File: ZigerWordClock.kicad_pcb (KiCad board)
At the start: 2 copper layers, 237 x 237 mm, 21 parts, among them U1 BH1750, U10 BTF-5V-060L-B_SK9822_LED_Stri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, U11 BTF-5V-060L-B_SK9822_LED_Stri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, U12 BTF-5V-060L-B_SK9822_LED_Stri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, U13 BTF-5V-060L-B_SK9822_LED_Stri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, U14 BTF-5V-060L-B_SK9822_LED_Stri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, U15 BTF-5V-060L-B_SK9822_LED_Stri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, U16 BTF-5V-060L-B_SK9822_LED_Stri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, U17 BTF-5V-060L-B_SK9822_LED_Stri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, U18 BTF-5V-060L-B_SK9822_LED_Stri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, U19 BTF-5V-060L-B_SK9822_LED_Stri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, U2 LILYGO(R)_TTGO_T8_ESP32-S2_V1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, U3 BTF-5V-060L-B_SK9822_LED_Stri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, U4 LevelShifter, U5 BTF-5V-060L-B_SK9822_LED_Stri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, U6 BTF-5V-060L-B_SK9822_LED_Stri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, U7 BTF-5V-060L-B_SK9822_LED_Stri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, U8 BTF-5V-060L-B_SK9822_LED_Stri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, U9 BTF-5V-060L-B_SK9822_LED_Stri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

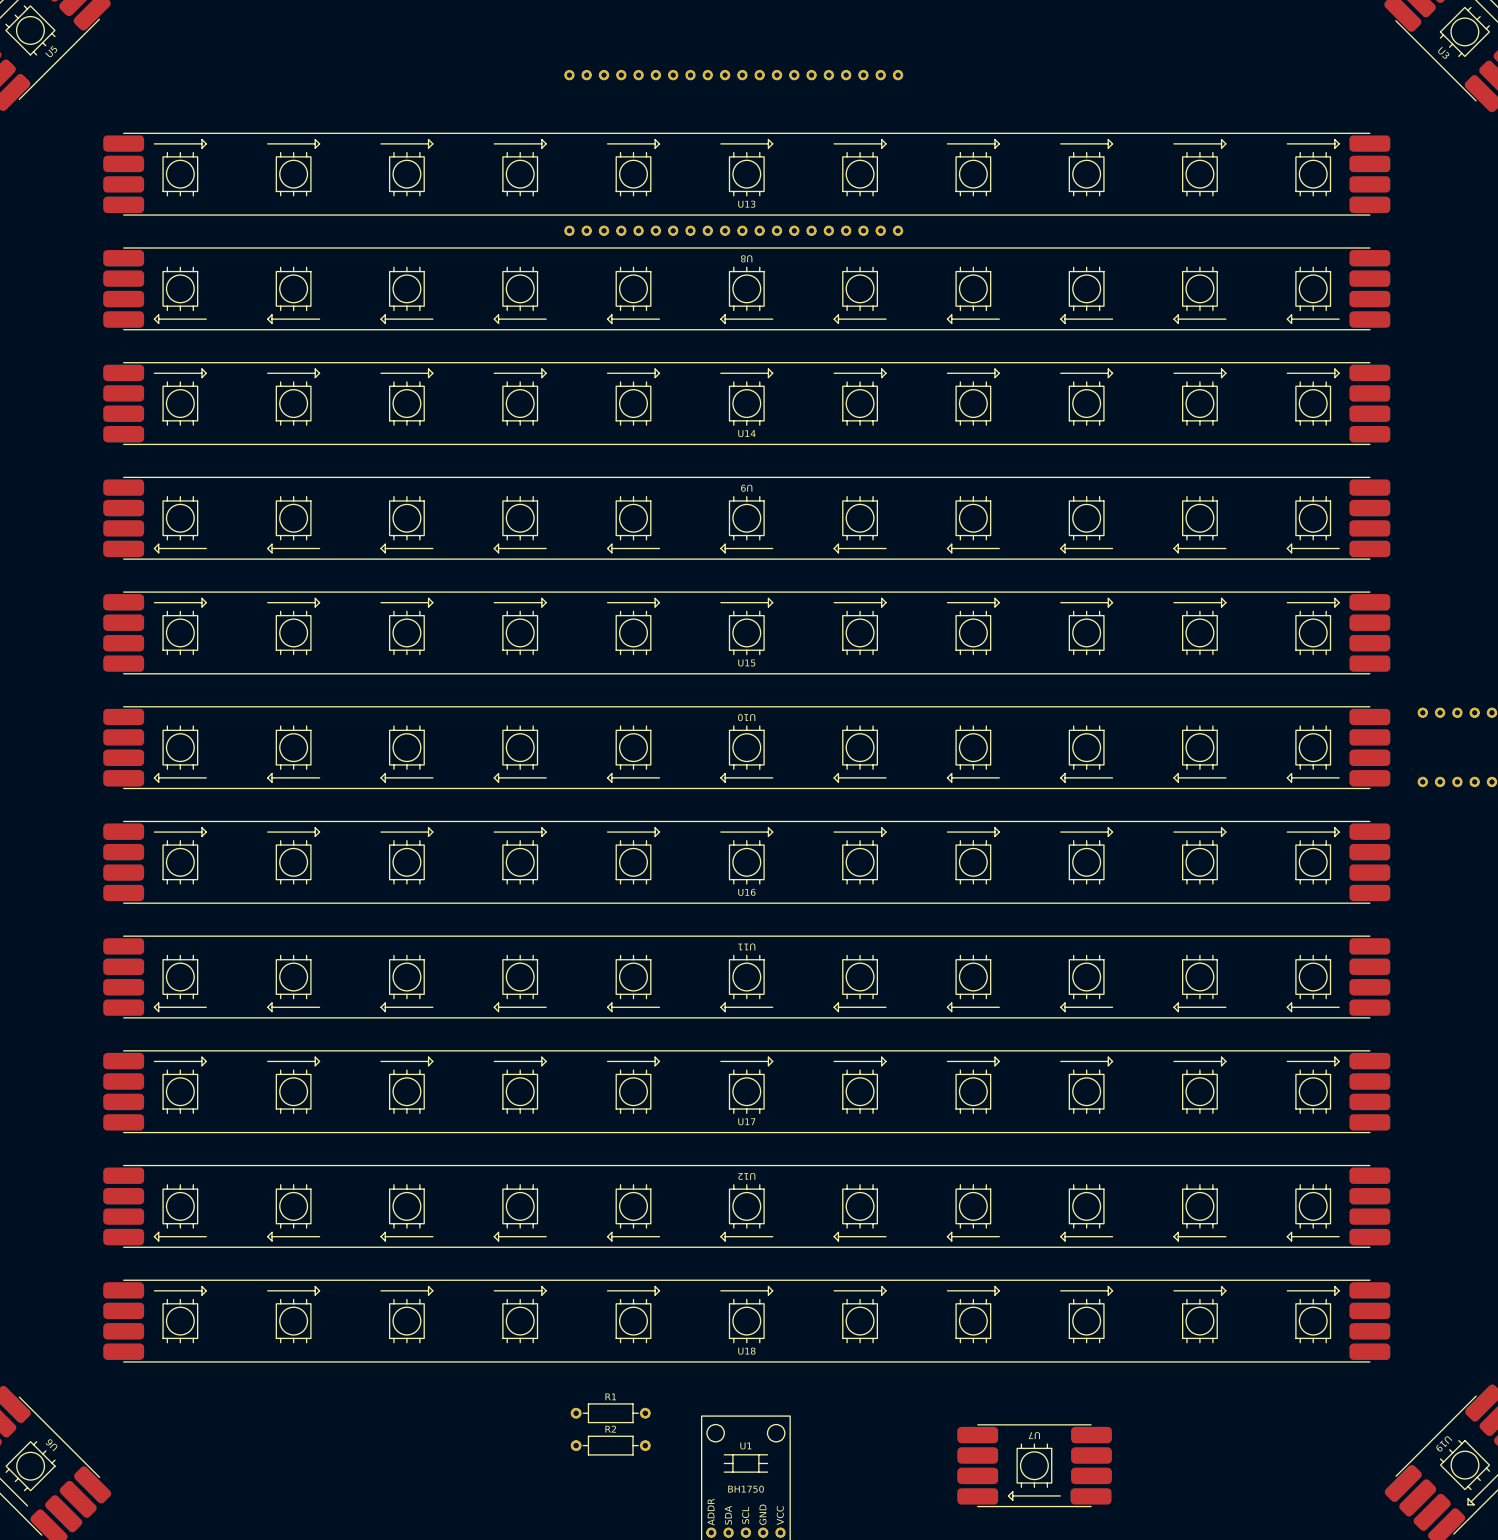
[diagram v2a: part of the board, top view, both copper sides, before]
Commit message: Adds ir receiver to schematic and board
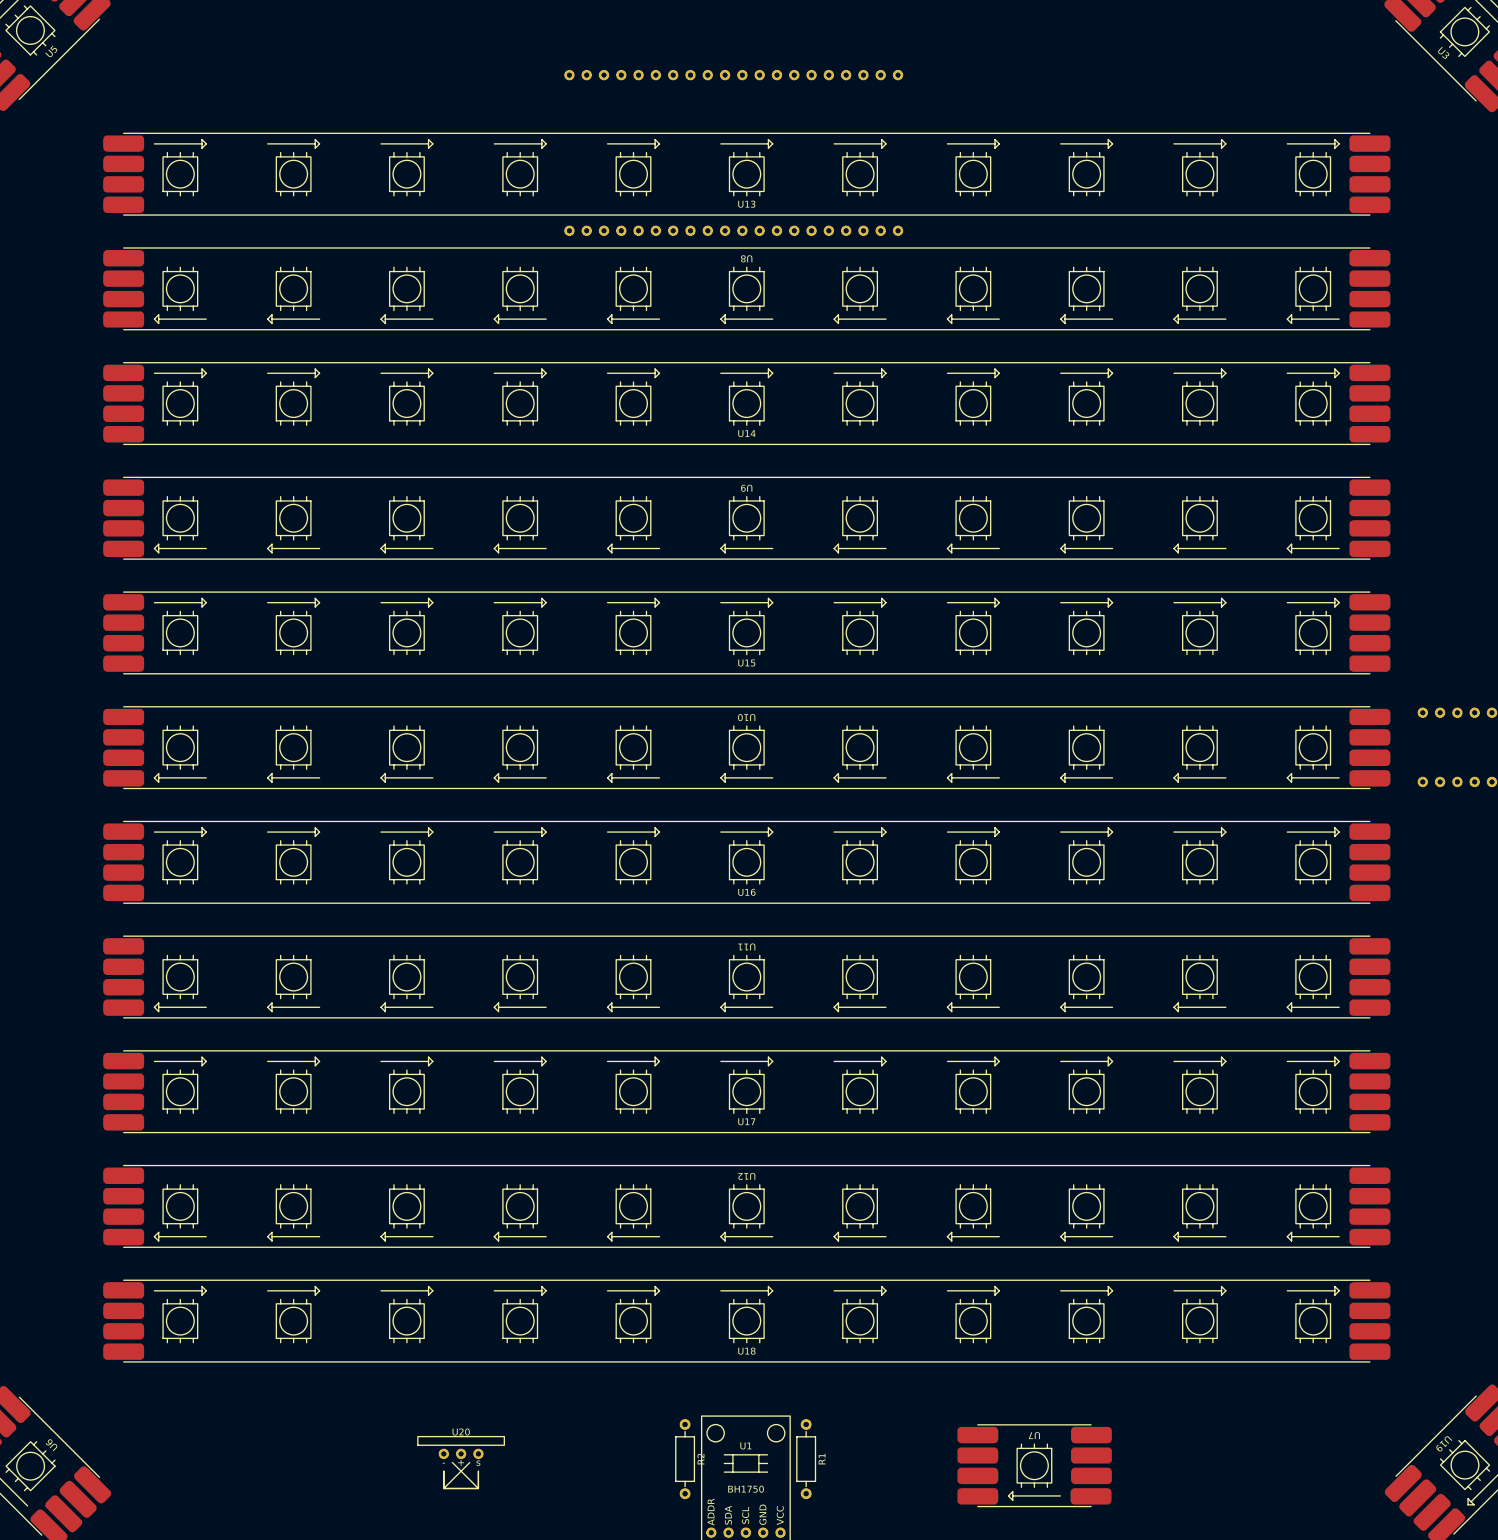
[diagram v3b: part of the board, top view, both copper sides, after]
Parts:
- added U20: IR-Module_38KHz, WordClock Footprint Library:IR-Module_38KHz, F.Cu at (118.2, 250.7)
- moved R1 33.8 mm to (168.9, 248.9), turned to -90 degrees
- moved R2 16.3 mm to (151.1, 248.9), turned to -90 degrees

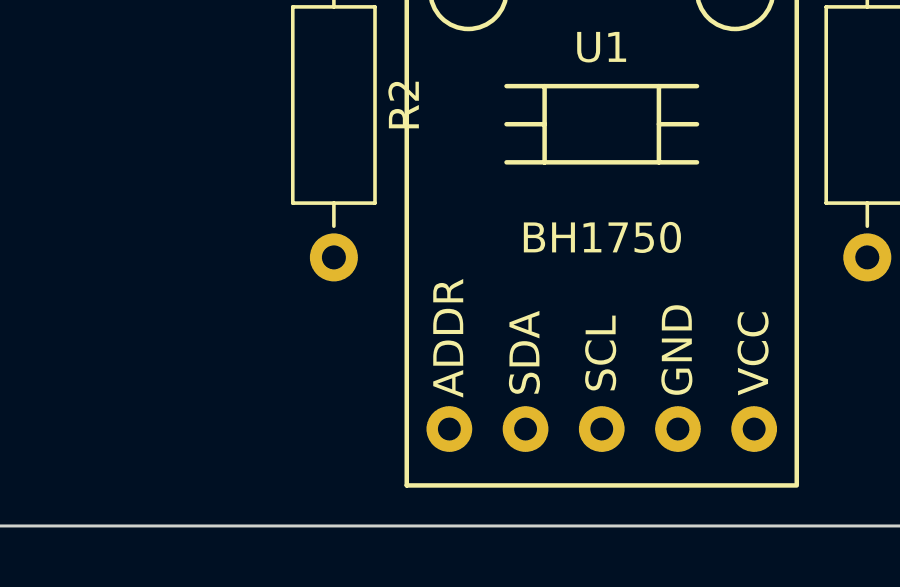
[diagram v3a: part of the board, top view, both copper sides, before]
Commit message: Added some connections
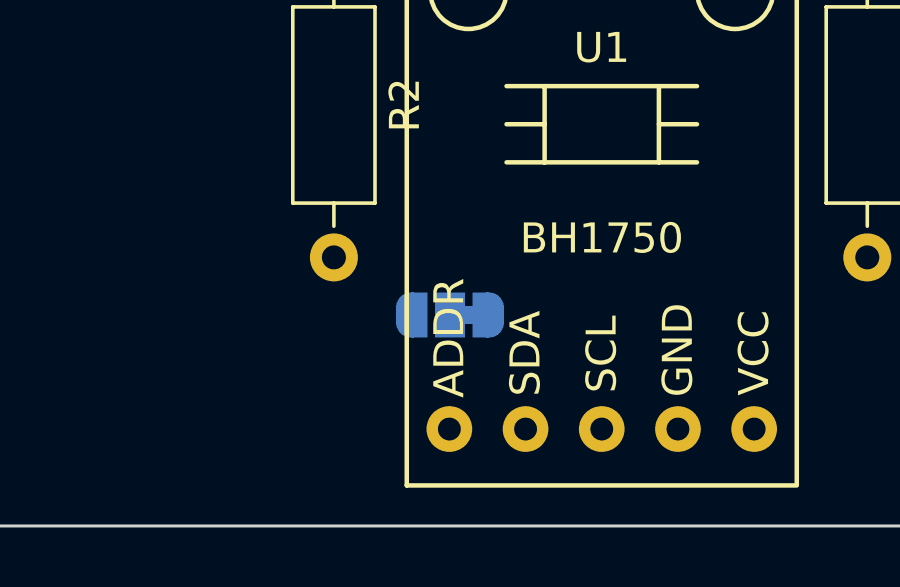
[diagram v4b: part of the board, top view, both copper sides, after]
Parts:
- added JP1: SolderJumper_3_Bridged12, Jumper:SolderJumper-3_P1.3mm_Bridged12_RoundedPad1.0x1.5mm_NumberLabels, B.Cu at (155.0, 261.0)
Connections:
- net CI renamed LED_CI
- net DI renamed LED_DI
- R1 pad 1: unconnected-(R1-Pad1) -> +3V3
- R2 pad 1: unconnected-(R2-Pad1) -> +3V3
- U1 pad ADDR: GND -> Net-(U1-PadADDR)
- U1 pad VCC: unconnected-(U1-PadVCC) -> +3V3
- U20 pad 3: unconnected-(U20-Pad3) -> IR_SIG
- U4 pad 10: unconnected-(U4-Pad10) -> +3V3
- U4 pad 2: unconnected-(U4-Pad2) -> IR_SIG
